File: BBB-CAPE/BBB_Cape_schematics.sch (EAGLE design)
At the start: 26 parts, among them IC1 EEPROM-I2CSMD

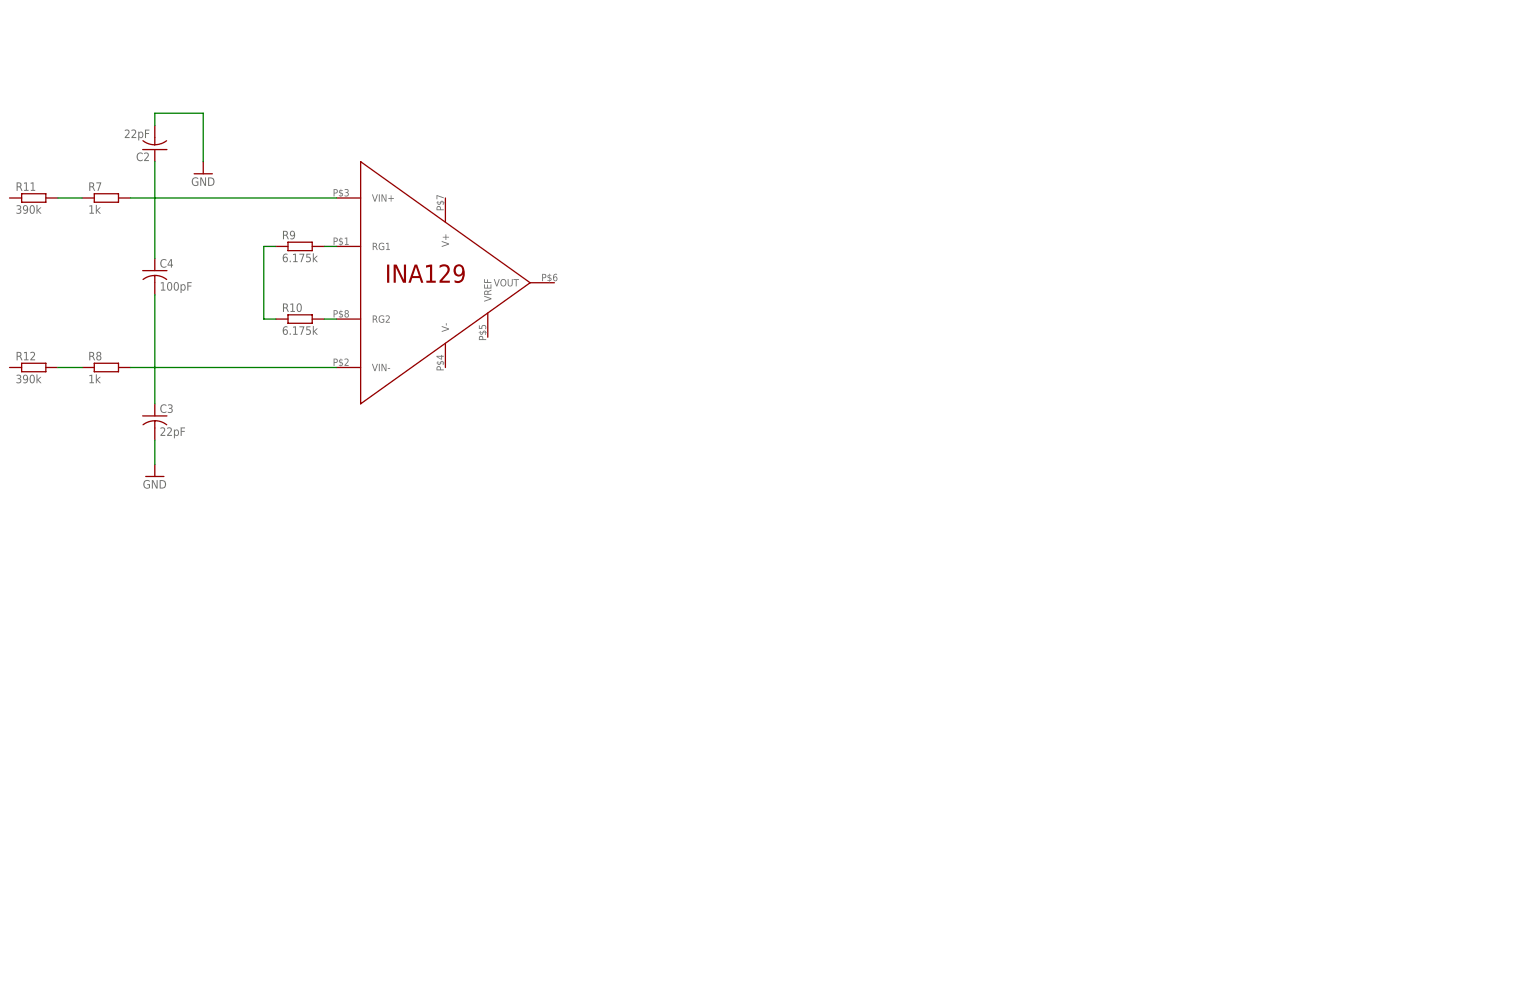
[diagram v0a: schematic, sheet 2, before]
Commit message: Added RLD amp, +2.5V Ref and -5V generator circuit
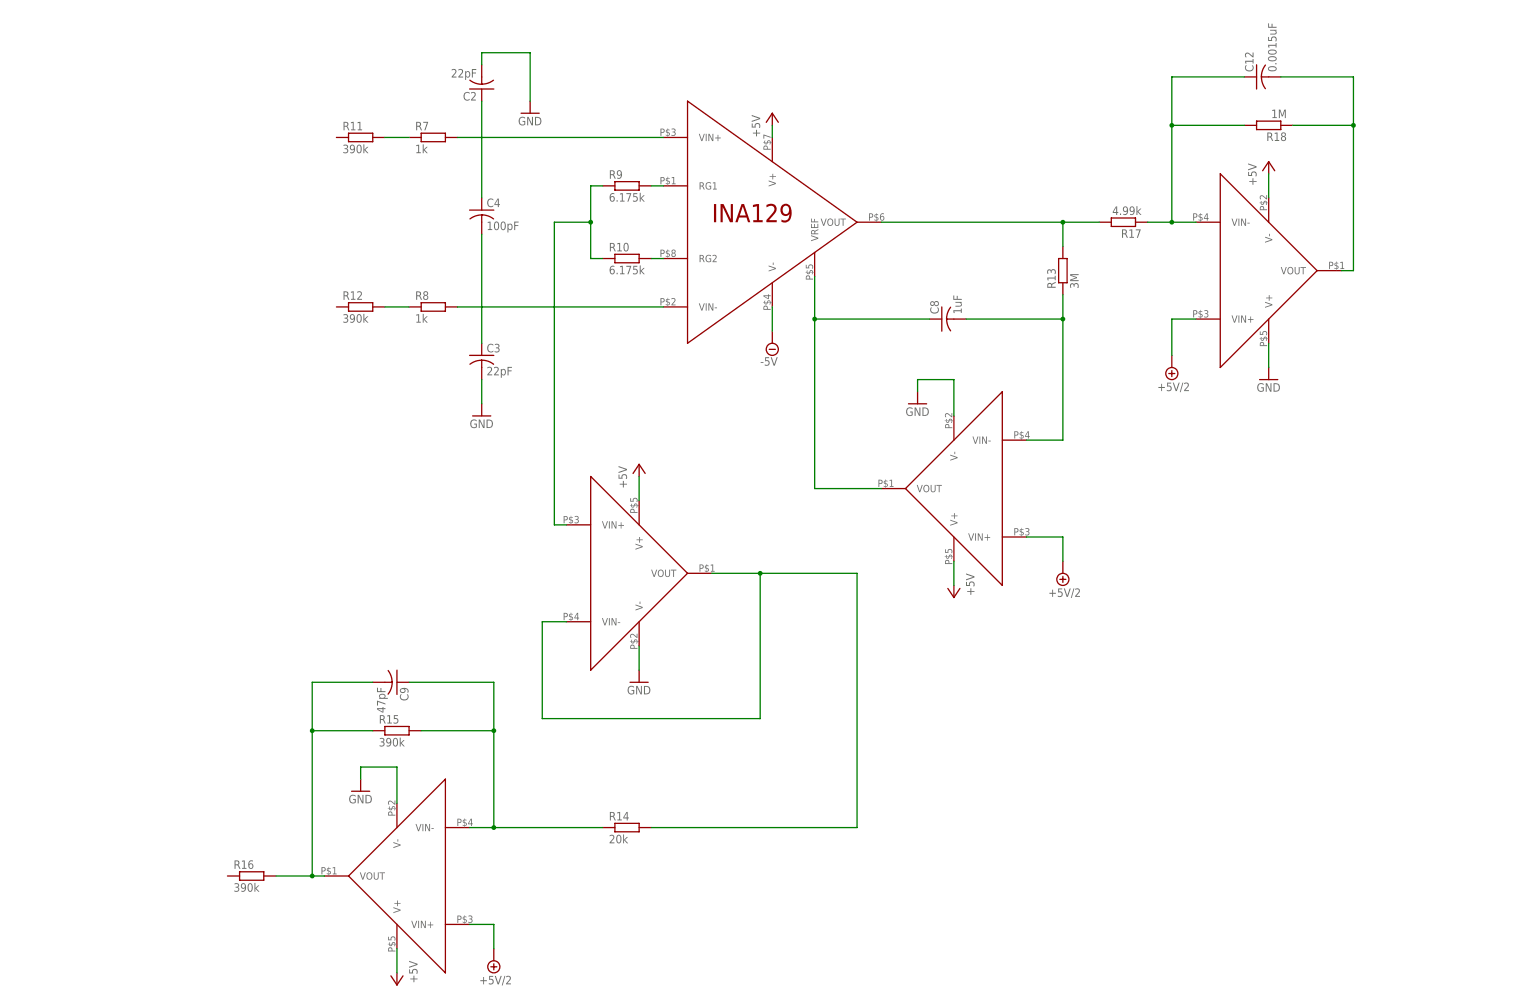
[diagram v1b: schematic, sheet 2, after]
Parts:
- added C10, C11, C9: 47pF, rcl:C-USC1206
- added C12: 0.0015uF, rcl:C-USC1206
- added C8: 1uF, rcl:C-USC1206
- added R13: 3M, resistor:R-EU_M1206
- added R14: 20k, resistor:R-EU_M1206
- added R15, R16: 390k, resistor:R-EU_M1206
- added R17: 4.99k, resistor:R-EU_M1206
- added R18: 1M, resistor:R-EU_M1206
- added U$10: REF5025, Components:REF5025
- added U$11, U$12, U$13, U$14, U$9: LMP2021, Components:LMP2021
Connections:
- new net +5V: C10.1, U$10.VIN, U$11.V+, U$12.V+, U$13.V-, U$4.V+, U$9.V+
- new net +5V/2: C11.1, U$10.VOUT, U$12.VIN+, U$13.VIN+, U$9.VIN+
- new net N$10: C8.1, U$4.VREF, U$9.VOUT
- new net N$11: R13.2, R17.2, U$4.VOUT
- new net N$12: C8.2, R13.1, U$9.VIN-
- new net N$16: R14.2, U$11.VIN-, U$11.VOUT
- new net N$17: C9.1, R14.1, R15.2, U$12.VIN-
- new net N$18: C12.1, R17.1, R18.2, U$13.VIN-
- new net N$19: C9.2, R15.1, R16.2, U$12.VOUT
- new net N$20: C12.2, R18.1, U$13.VOUT
- new net N$21: C6.1, U$14.V-, U$14.VIN+, U$5.OUT
- net -5V: now also U$14.VIN-, U$14.VOUT, U$4.V-; no longer C6.1, U$5.OUT
- net 5V: now also U$14.V+
- net GND: now also C10.2, C11.2, U$10.GND, U$11.V-, U$12.V-, U$13.V+, U$9.V-
- net N$5: now also U$11.VIN+
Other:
- moved on the sheet: C2, C3, C4, R10, R11, R12, R7, R8, R9

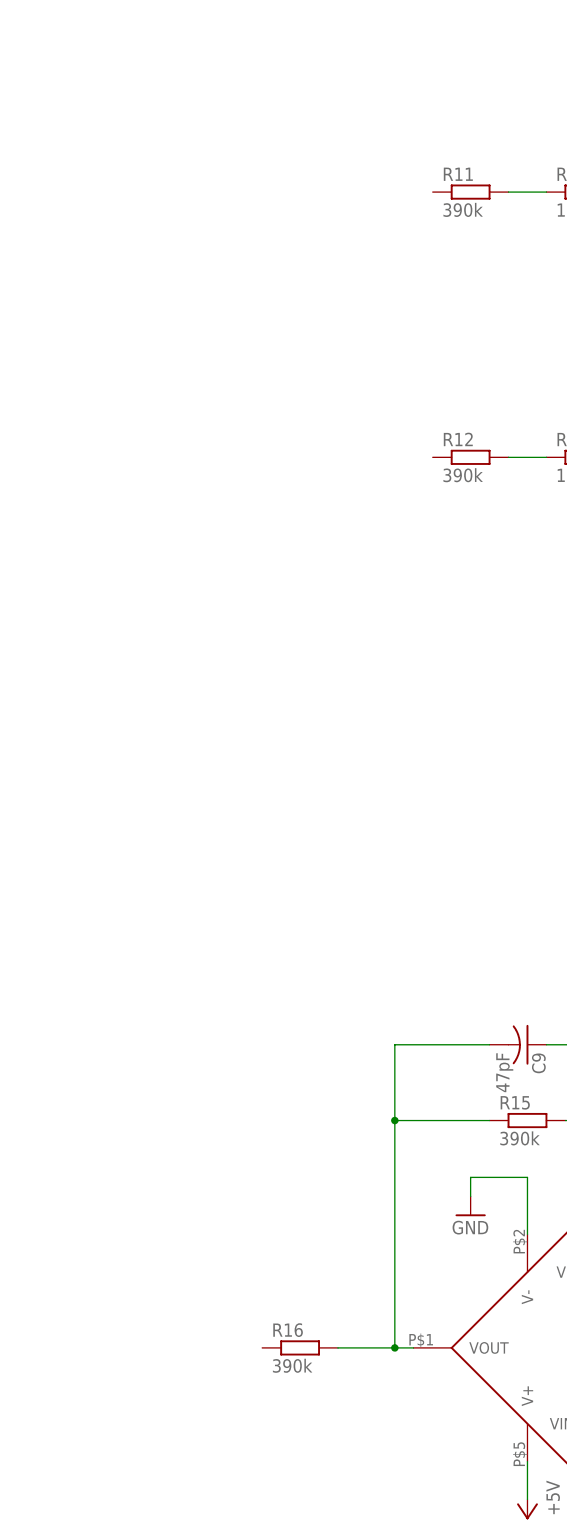
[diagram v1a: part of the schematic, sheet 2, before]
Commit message: added device symbol and footprint for finger and thumb PAD
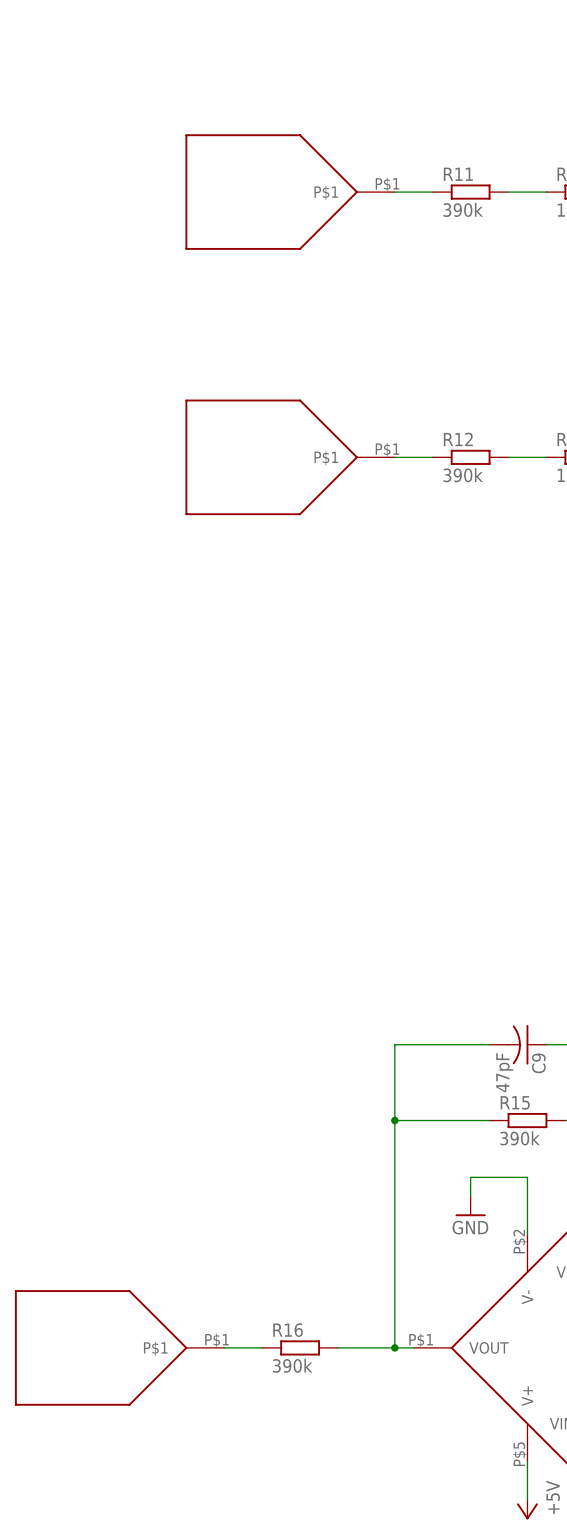
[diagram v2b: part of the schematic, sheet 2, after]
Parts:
- added U$16, U$17, U$18: PAD, Components:PAD
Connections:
- new net N$22: R16.1, U$18.P$1
- new net N$23: R11.1, U$16.P$1
- new net N$24: R12.1, U$17.P$1
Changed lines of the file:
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@@
 <grid distance="0.1" unitdist="inch" unit="inch" style="lines" multiple="1" display="yes" altdistance="0.01" altunitdist="inch" altunit="inch"/>
 <layers>
-<layer number="1" name="Top" color="4" fill="1" visible="yes" active="no"/>
-<layer number="2" name="Route2" color="1" fill="3" visible="yes" active="no"/>
-<layer number="3" name="Route3" color="4" fill="3" visible="yes" active="no"/>
-<layer number="4" name="Route4" color="1" fill="4" visible="yes" active="no"/>
-<layer number="5" name="Route5" color="4" fill="4" visible="yes" active="no"/>
-<layer number="6" name="Route6" color="1" fill="8" visible="yes" active="no"/>
-<layer number="7" name="Route7" color="4" fill="8" visible="yes" active="no"/>
-<layer number="8" name="Route8" color="1" fill="2" visible="yes" active="no"/>
-<layer number="9" name="Route9" color="4" fill="2" visible="yes" active="no"/>
-<layer number="10" name="Route10" color="1" fill="7" visible="yes" active="no"/>
-<layer number="11" name="Route11" color="4" fill="7" visible="yes" active="no"/>
-<layer number="12" name="Route12" color="1" fill="5" visible="yes" active="no"/>
-<layer number="13" name="Route13" color="4" fill="5" visible="yes" active="no"/>
-<layer number="14" name="Route14" color="1" fill="6" visible="yes" active="no"/>
-<layer number="15" name="Route15" color="4" fill="6" visible="yes" active="no"/>
-<layer number="16" name="Bottom" color="1" fill="1" visible="yes" active="no"/>
-<layer number="17" name="Pads" color="2" fill="1" visible="yes" active="no"/>
-<layer number="18" name="Vias" color="2" fill="1" visible="yes" active="no"/>
-<layer number="19" name="Unrouted" color="6" fill="1" visible="yes" active="no"/>
-<layer number="20" name="Dimension" color="15" fill="1" visible="yes" active="no"/>
-<layer number="21" name="tPlace" color="7" fill="1" visible="yes" active="no"/>
-<layer number="22" name="bPlace" color="7" fill="1" visible="yes" active="no"/>
-<layer number="23" name="tOrigins" color="15" fill="1" visible="yes" active="no"/>
-<layer number="24" name="bOrigins" color="15" fill="1" visible="yes" active="no"/>
-<layer number="25" name="tNames" color="7" fill="1" visible="yes" active="no"/>
-<layer number="26" name="bNames" color="7" fill="1" visible="yes" active="no"/>
-<layer number="27" name="tValues" color="7" fill="1" visible="yes" active="no"/>
-<layer number="28" name="bValues" color="7" fill="1" visible="yes" active="no"/>
+<layer number="1" name="Top" color="4" fill="1" visible="no" active="no"/>
+<layer number="2" name="Route2" color="1" fill="3" visible="no" active="no"/>
+<layer number="3" name="Route3" color="4" fill="3" visible="no" active="no"/>
+<layer number="4" name="Route4" color="1" fill="4" visible="no" active="no"/>
+<layer number="5" name="Route5" color="4" fill="4" visible="no" active="no"/>
+<layer number="6" name="Route6" color="1" fill="8" visible="no" active="no"/>
+<layer number="7" name="Route7" color="4" fill="8" visible="no" active="no"/>
+<layer number="8" name="Route8" color="1" fill="2" visible="no" active="no"/>
+<layer number="9" name="Route9" color="4" fill="2" visible="no" active="no"/>
+<layer number="10" name="Route10" color="1" fill="7" visible="no" active="no"/>
+<layer number="11" name="Route11" color="4" fill="7" visible="no" active="no"/>
+<layer number="12" name="Route12" color="1" fill="5" visible="no" active="no"/>
+<layer number="13" name="Route13" color="4" fill="5" visible="no" active="no"/>
+<layer number="14" name="Route14" color="1" fill="6" visible="no" active="no"/>
+<layer number="15" name="Route15" color="4" fill="6" visible="no" active="no"/>
+<layer number="16" name="Bottom" color="1" fill="1" visible="no" active="no"/>
+<layer number="17" name="Pads" color="2" fill="1" visible="no" active="no"/>
+<layer number="18" name="Vias" color="2" fill="1" visible="no" active="no"/>
+<layer number="19" name="Unrouted" color="6" fill="1" visible="no" active="no"/>
+<layer number="20" name="Dimension" color="15" fill="1" visible="no" active="no"/>
+<layer number="21" name="tPlace" color="7" fill="1" visible="no" active="no"/>
+<layer number="22" name="bPlace" color="7" fill="1" visible="no" active="no"/>
+<layer number="23" name="tOrigins" color="15" fill="1" visible="no" active="no"/>
+<layer number="24" name="bOrigins" color="15" fill="1" visible="no" active="no"/>
+<layer number="25" name="tNames" color="7" fill="1" visible="no" active="no"/>
+<layer number="26" name="bNames" color="7" fill="1" visible="no" active="no"/>
+<layer number="27" name="tValues" color="7" fill="1" visible="no" active="no"/>
+<layer number="28" name="bValues" color="7" fill="1" visible="no" active="no"/>
 <layer number="29" name="tStop" color="7" fill="3" visible="no" active="no"/>
 <layer number="30" name="bStop" color="7" fill="6" visible="no" active="no"/>
@@
 <layer number="35" name="tGlue" color="7" fill="4" visible="no" active="no"/>
 <layer number="36" name="bGlue" color="7" fill="5" visible="no" active="no"/>
-<layer number="37" name="tTest" color="7" fill="1" visible="yes" active="no"/>
-<layer number="38" name="bTest" color="7" fill="1" visible="yes" active="no"/>
+<layer number="37" name="tTest" color="7" fill="1" visible="no" active="no"/>
+<layer number="38" name="bTest" color="7" fill="1" visible="no" active="no"/>
 <layer number="39" name="tKeepout" color="4" fill="11" visible="no" active="no"/>
 <layer number="40" name="bKeepout" color="1" fill="11" visible="no" active="no"/>
@@
 <layer number="44" name="Drills" color="7" fill="1" visible="no" active="no"/>
 <layer number="45" name="Holes" color="7" fill="1" visible="no" active="no"/>
-<layer number="46" name="Milling" color="3" fill="1" visible="yes" active="no"/>
-<layer number="47" name="Measures" color="7" fill="1" visible="yes" active="no"/>
-<layer number="48" name="Document" color="7" fill="1" visible="yes" active="no"/>
-<layer number="49" name="Reference" color="7" fill="1" visible="yes" active="no"/>
-<layer number="50" name="dxf" color="7" fill="1" visible="yes" active="no"/>
-<layer number="51" name="tDocu" color="7" fill="1" visible="yes" active="no"/>
-<layer number="52" name="bDocu" color="7" fill="1" visible="yes" active="no"/>
-<layer number="53" name="tGND_GNDA" color="7" fill="9" visible="yes" active="no"/>
-<layer number="54" name="bGND_GNDA" color="1" fill="9" visible="yes" active="no"/>
-<layer number="56" name="wert" color="7" fill="1" visible="yes" active="no"/>
+<layer number="46" name="Milling" color="3" fill="1" visible="no" active="no"/>
+<layer number="47" name="Measures" color="7" fill="1" visible="no" active="no"/>
+<layer number="48" name="Document" color="7" fill="1" visible="no" active="no"/>
+<layer number="49" name="Reference" color="7" fill="1" visible="no" active="no"/>
+<layer number="50" name="dxf" color="7" fill="1" visible="no" active="no"/>
+<layer number="51" name="tDocu" color="7" fill="1" visible="no" active="no"/>
+<layer number="52" name="bDocu" color="7" fill="1" visible="no" active="no"/>
+<layer number="53" name="tGND_GNDA" color="7" fill="9" visible="no" active="no"/>
+<layer number="54" name="bGND_GNDA" color="1" fill="9" visible="no" active="no"/>
+<layer number="56" name="wert" color="7" fill="1" visible="no" active="no"/>
 <layer number="91" name="Nets" color="2" fill="1" visible="yes" active="yes"/>
 <layer number="92" name="Busses" color="1" fill="1" visible="yes" active="yes"/>
@@
 <part name="U$14" library="Components" deviceset="LMP2021" device=""/>
 <part name="U$15" library="SparkFun-Aesthetics" deviceset="5V" device=""/>
+<part name="U$16" library="Components" deviceset="PAD" device=""/>
+<part name="U$17" library="Components" deviceset="PAD" device=""/>
+<part name="U$18" library="Components" deviceset="PAD" device=""/>
 </parts>
 <sheets>
@@
 <instance part="P+10" gate="1" x="287.02" y="200.66"/>
 <instance part="GND19" gate="1" x="287.02" y="154.94"/>
+<instance part="U$16" gate="G$1" x="68.58" y="205.74"/>
+<instance part="U$17" gate="G$1" x="68.58" y="170.18"/>
+<instance part="U$18" gate="G$1" x="45.72" y="50.8"/>
 </instances>
 <busses>
@@
 </segment>
 </net>
+<net name="N$22" class="0">
+<segment>
+<pinref part="U$18" gate="G$1" pin="P$1"/>
+<pinref part="R16" gate="G$1" pin="1"/>
+<wire x1="63.5" y1="50.8" x2="68.58" y2="50.8" width="0.1524" layer="91"/>
+</segment>
+</net>
+<net name="N$23" class="0">
+<segment>
+<pinref part="U$16" gate="G$1" pin="P$1"/>
+<pinref part="R11" gate="G$1" pin="1"/>
+<wire x1="86.36" y1="205.74" x2="91.44" y2="205.74" width="0.1524" layer="91"/>
+</segment>
+</net>
+<net name="N$24" class="0">
+<segment>
+<pinref part="U$17" gate="G$1" pin="P$1"/>
+<pinref part="R12" gate="G$1" pin="1"/>
+<wire x1="86.36" y1="170.18" x2="91.44" y2="170.18" width="0.1524" layer="91"/>
+</segment>
+</net>

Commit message: removed REF5025 IC from schematic, instead using REF3125 to generate 2.5V reference voltage
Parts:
- removed C10, C11: 47pF, rcl:C-USC1206
- removed U$10: REF5025, Components:REF5025
- added C13, C14, C16, C19: 0.1uF, rcl:C-USC1206
- added C15, C18: 10uF, rcl:C-USC1206
- added C17: 0.10uF, rcl:C-USC1206
- added R19: 100k, resistor:R-EU_M1206
- added TP1_2.5V, TP1_MIN5V, TP2_2.5V, TP2_MIN5V, TP_3.3V, TP_5V, TP_ECG_INA, TP_ECG_LPF, TP_INA_VREF: TPB2,54, testpad:TPB2,54
- added U$19: ADS1252, Components:ADS1252
- added U$21: REF3125, Components:REF3125
- added U$22: OPA353, Components:OPA353
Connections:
- new net N$25: C14.1, R19.1, U$21.VOUT
- new net N$26: C15.1, C16.1, R19.2, TP1_2.5V.TP, U$22.VIN+
- net +5V: now also C13.1, C17.1, U$21.VIN, U$22.V-; no longer C10.1, U$10.VIN
- net +5V/2: now also C18.1, C19.1, TP2_2.5V.TP, U$19.VIN-, U$19.VREF, U$22.VIN-, U$22.VOUT; no longer C11.1, U$10.VOUT
- net -5V: now also TP2_MIN5V.TP
- net 3.3V: now also TP_3.3V.TP
- net 5V: now also TP_5V.TP, U$19.V+
- net GND: now also C13.2, C14.2, C15.2, C16.2, C17.2, C18.2, C19.2, U$19.GND, U$21.GND, U$22.V+; no longer C10.2, C11.2, U$10.GND
- net N$10: now also TP_INA_VREF.TP
- net N$11: now also TP_ECG_INA.TP
- net N$20: now also TP_ECG_LPF.TP, U$19.VIN+
- net N$21: now also TP1_MIN5V.TP
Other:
- note added: "ECG_LPF"
- note added: "REF31253"
